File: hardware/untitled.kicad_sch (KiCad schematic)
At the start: 12 parts, among them J1 FH35C-25S-0.3SHW_50_, J8 FH35C-25S-0.3SHW_50_

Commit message: fixed details
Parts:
- TP32, TP33, TP34, TP35, TP36, TP37, TP38, TP39, TP40, TP41: footprint TestPoint:TestPoint_Pad_0.8x0.8mm -> TestPoint:TestPoint_Pad_1.0x1.0mm
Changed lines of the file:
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@@
       (effects (font (size 1.27 1.27)))
     )
-    (property "Footprint" "TestPoint:TestPoint_Pad_0.8x0.8mm" (at 56.515 92.71 0)
+    (property "Footprint" "TestPoint:TestPoint_Pad_1.0x1.0mm" (at 56.515 92.71 0)
       (effects (font (size 1.27 1.27)) hide)
     )
@@
       (effects (font (size 1.27 1.27)))
     )
-    (property "Footprint" "TestPoint:TestPoint_Pad_0.8x0.8mm" (at 56.515 113.03 0)
+    (property "Footprint" "TestPoint:TestPoint_Pad_1.0x1.0mm" (at 56.515 113.03 0)
       (effects (font (size 1.27 1.27)) hide)
     )
@@
       (effects (font (size 1.27 1.27)))
     )
-    (property "Footprint" "TestPoint:TestPoint_Pad_0.8x0.8mm" (at 56.515 97.79 0)
+    (property "Footprint" "TestPoint:TestPoint_Pad_1.0x1.0mm" (at 56.515 97.79 0)
       (effects (font (size 1.27 1.27)) hide)
     )
@@
       (effects (font (size 1.27 1.27)))
     )
-    (property "Footprint" "TestPoint:TestPoint_Pad_0.8x0.8mm" (at 56.515 115.57 0)
+    (property "Footprint" "TestPoint:TestPoint_Pad_1.0x1.0mm" (at 56.515 115.57 0)
       (effects (font (size 1.27 1.27)) hide)
     )
@@
       (effects (font (size 1.27 1.27)))
     )
-    (property "Footprint" "TestPoint:TestPoint_Pad_0.8x0.8mm" (at 56.515 105.41 0)
+    (property "Footprint" "TestPoint:TestPoint_Pad_1.0x1.0mm" (at 56.515 105.41 0)
       (effects (font (size 1.27 1.27)) hide)
     )
@@
       (effects (font (size 1.27 1.27)))
     )
-    (property "Footprint" "TestPoint:TestPoint_Pad_0.8x0.8mm" (at 56.515 95.25 0)
+    (property "Footprint" "TestPoint:TestPoint_Pad_1.0x1.0mm" (at 56.515 95.25 0)
       (effects (font (size 1.27 1.27)) hide)
     )
@@
       (effects (font (size 1.27 1.27)))
     )
-    (property "Footprint" "TestPoint:TestPoint_Pad_0.8x0.8mm" (at 56.515 107.95 0)
+    (property "Footprint" "TestPoint:TestPoint_Pad_1.0x1.0mm" (at 56.515 107.95 0)
       (effects (font (size 1.27 1.27)) hide)
     )
@@
       (effects (font (size 1.27 1.27)))
     )
-    (property "Footprint" "TestPoint:TestPoint_Pad_0.8x0.8mm" (at 56.515 110.49 0)
+    (property "Footprint" "TestPoint:TestPoint_Pad_1.0x1.0mm" (at 56.515 110.49 0)
       (effects (font (size 1.27 1.27)) hide)
     )
@@
       (effects (font (size 1.27 1.27)))
     )
-    (property "Footprint" "TestPoint:TestPoint_Pad_0.8x0.8mm" (at 56.515 102.87 0)
+    (property "Footprint" "TestPoint:TestPoint_Pad_1.0x1.0mm" (at 56.515 102.87 0)
       (effects (font (size 1.27 1.27)) hide)
     )
@@
       (effects (font (size 1.27 1.27)))
     )
-    (property "Footprint" "TestPoint:TestPoint_Pad_0.8x0.8mm" (at 56.515 100.33 0)
-      (effects (font (size 1.27 1.27)) hide)
-    )
+    (property "Footprint" "TestPoint:TestPoint_Pad_1.0x1.0mm" (at 56.515 100.33 0)
+      (effects (font (size 1.27 1.27)) hide)
+    )

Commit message: fixed some 3d models + redid power distribution on the BOE board
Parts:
- TP32, TP33, TP34, TP35, TP36, TP37, TP38, TP39, TP40, TP41: footprint TestPoint:TestPoint_Pad_1.0x1.0mm -> mylib:myTestpoint
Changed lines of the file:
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@@
       (effects (font (size 1.27 1.27)))
     )
-    (property "Footprint" "TestPoint:TestPoint_Pad_1.0x1.0mm" (at 56.515 92.71 0)
+    (property "Footprint" "mylib:myTestpoint" (at 56.515 92.71 0)
       (effects (font (size 1.27 1.27)) hide)
     )
@@
       (effects (font (size 1.27 1.27)))
     )
-    (property "Footprint" "TestPoint:TestPoint_Pad_1.0x1.0mm" (at 56.515 113.03 0)
+    (property "Footprint" "mylib:myTestpoint" (at 56.515 113.03 0)
       (effects (font (size 1.27 1.27)) hide)
     )
@@
       (effects (font (size 1.27 1.27)))
     )
-    (property "Footprint" "TestPoint:TestPoint_Pad_1.0x1.0mm" (at 56.515 97.79 0)
+    (property "Footprint" "mylib:myTestpoint" (at 56.515 97.79 0)
       (effects (font (size 1.27 1.27)) hide)
     )
@@
       (effects (font (size 1.27 1.27)))
     )
-    (property "Footprint" "TestPoint:TestPoint_Pad_1.0x1.0mm" (at 56.515 115.57 0)
+    (property "Footprint" "mylib:myTestpoint" (at 56.515 115.57 0)
       (effects (font (size 1.27 1.27)) hide)
     )
@@
       (effects (font (size 1.27 1.27)))
     )
-    (property "Footprint" "TestPoint:TestPoint_Pad_1.0x1.0mm" (at 56.515 105.41 0)
+    (property "Footprint" "mylib:myTestpoint" (at 56.515 105.41 0)
       (effects (font (size 1.27 1.27)) hide)
     )
@@
       (effects (font (size 1.27 1.27)))
     )
-    (property "Footprint" "TestPoint:TestPoint_Pad_1.0x1.0mm" (at 56.515 95.25 0)
+    (property "Footprint" "mylib:myTestpoint" (at 56.515 95.25 0)
       (effects (font (size 1.27 1.27)) hide)
     )
@@
       (effects (font (size 1.27 1.27)))
     )
-    (property "Footprint" "TestPoint:TestPoint_Pad_1.0x1.0mm" (at 56.515 107.95 0)
+    (property "Footprint" "mylib:myTestpoint" (at 56.515 107.95 0)
       (effects (font (size 1.27 1.27)) hide)
     )
@@
       (effects (font (size 1.27 1.27)))
     )
-    (property "Footprint" "TestPoint:TestPoint_Pad_1.0x1.0mm" (at 56.515 110.49 0)
+    (property "Footprint" "mylib:myTestpoint" (at 56.515 110.49 0)
       (effects (font (size 1.27 1.27)) hide)
     )
@@
       (effects (font (size 1.27 1.27)))
     )
-    (property "Footprint" "TestPoint:TestPoint_Pad_1.0x1.0mm" (at 56.515 102.87 0)
+    (property "Footprint" "mylib:myTestpoint" (at 56.515 102.87 0)
       (effects (font (size 1.27 1.27)) hide)
     )
@@
       (effects (font (size 1.27 1.27)))
     )
-    (property "Footprint" "TestPoint:TestPoint_Pad_1.0x1.0mm" (at 56.515 100.33 0)
-      (effects (font (size 1.27 1.27)) hide)
-    )
+    (property "Footprint" "mylib:myTestpoint" (at 56.515 100.33 0)
+      (effects (font (size 1.27 1.27)) hide)
+    )

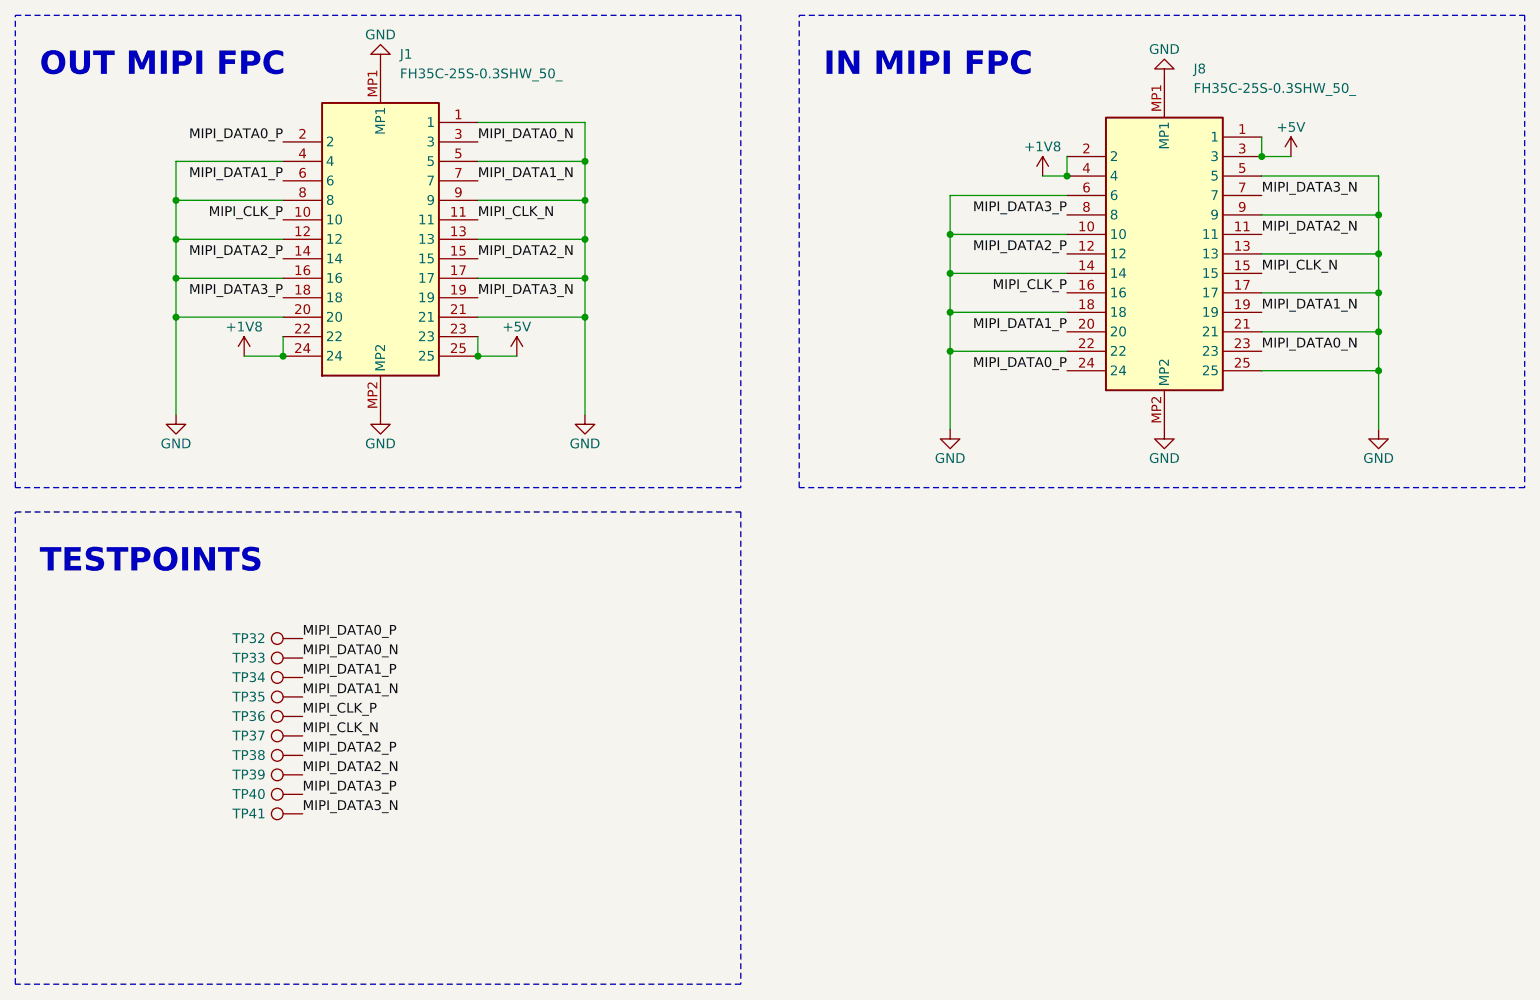
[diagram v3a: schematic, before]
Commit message: updated readme + fixed pcb + cleaned up code
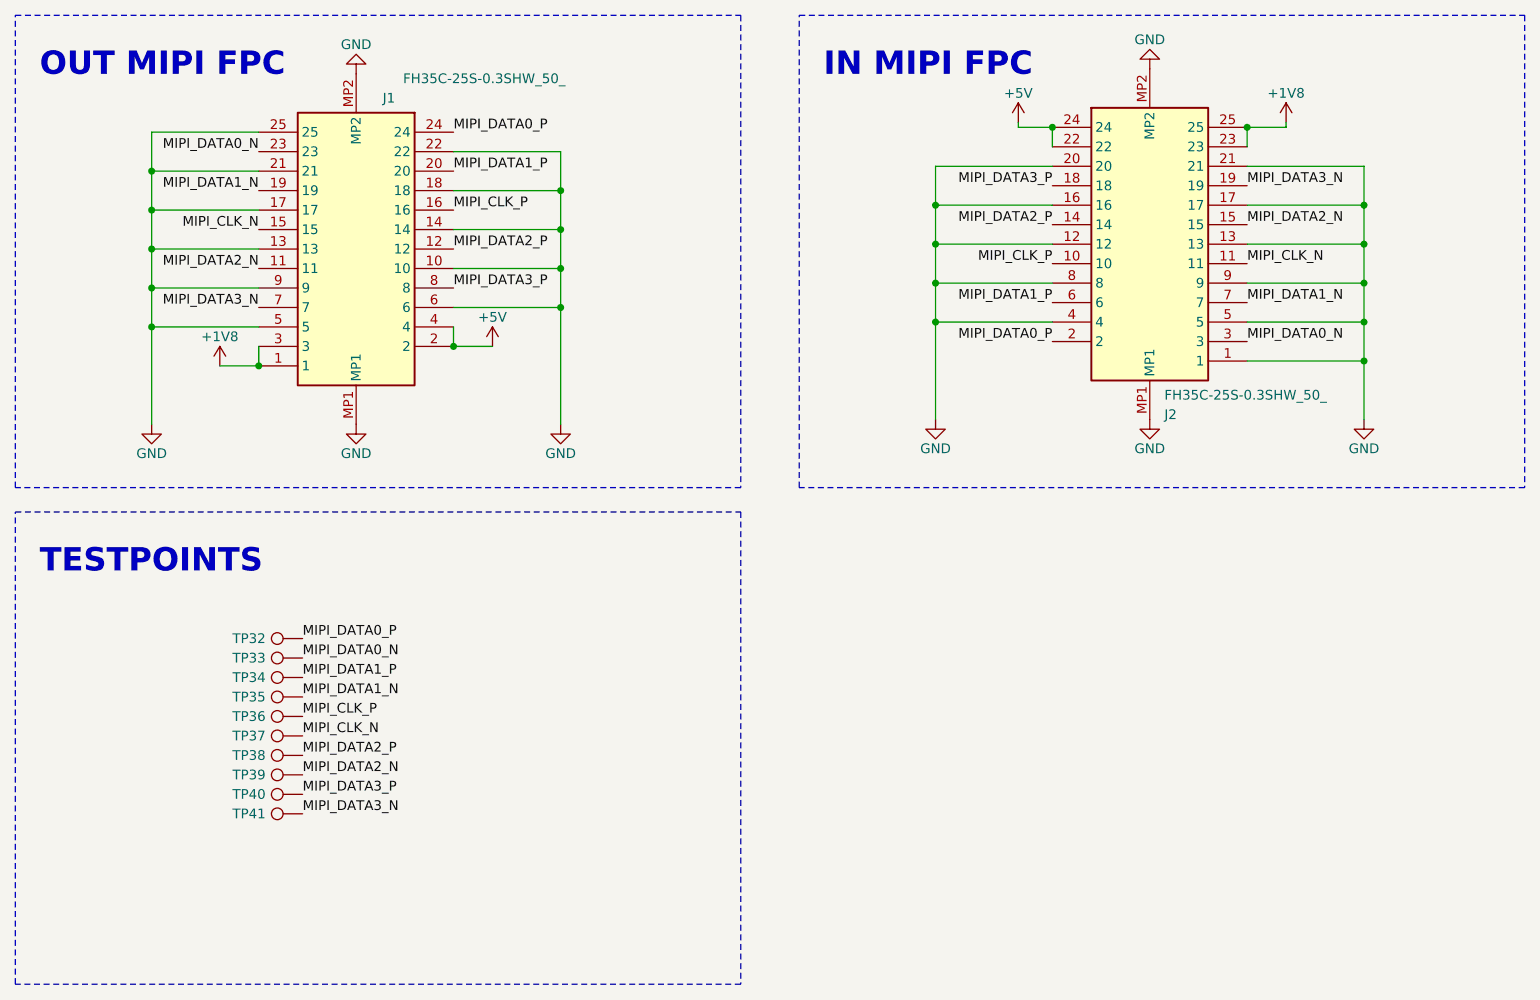
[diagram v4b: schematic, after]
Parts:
- removed J8: FH35C-25S-0.3SHW_50_, SamacSys_Parts:FH35C25S03SHW50, symbol SamacSys_Parts:FH35C-25S-0.3SHW_50_
- added J2: FH35C-25S-0.3SHW_50_, SamacSys_Parts:FH35C25S03SHW50, symbol SamacSys_Parts:FH35C-25S-0.3SHW_50_
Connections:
- net +1V8: now also J1.1, J1.3, J2.23, J2.25; no longer J1.22, J1.24
- net +5V: now also J1.2, J1.4, J2.22, J2.24; no longer J1.23, J1.25
- net GND: now also J1.10, J1.14, J1.18, J1.22, J1.25, J1.6, J2.1, J2.12, J2.13, J2.16, J2.17, J2.20, J2.21, J2.4, J2.5, J2.8, J2.9, J2.MP1, J2.MP2; no longer J1.1, J1.12, J1.16, J1.20, J1.4, J1.8
- net MIPI_CLK_N: now also J1.15, J2.11; no longer J1.11
- net MIPI_CLK_P: now also J1.16, J2.10; no longer J1.10
- net MIPI_DATA0_N: now also J1.23, J2.3; no longer J1.3
- net MIPI_DATA0_P: now also J1.24, J2.2; no longer J1.2
- net MIPI_DATA1_N: now also J1.19, J2.7; no longer J1.7
- net MIPI_DATA1_P: now also J1.20, J2.6; no longer J1.6
- net MIPI_DATA2_N: now also J1.11, J2.15; no longer J1.15
- net MIPI_DATA2_P: now also J1.12, J2.14; no longer J1.14
- net MIPI_DATA3_N: now also J1.7, J2.19; no longer J1.19
- net MIPI_DATA3_P: now also J1.8, J2.18; no longer J1.18
